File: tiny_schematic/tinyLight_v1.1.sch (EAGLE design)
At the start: 38 parts, among them IC1 NCP1117, IC2 XMEGA-A4TQFP, IC3 CM1293A-02SR, J1 RASM722PX, J2 Molex, J3 PDI, Q1 BC849SMD, Q2 BC849SMD, X1 MICRO-USB

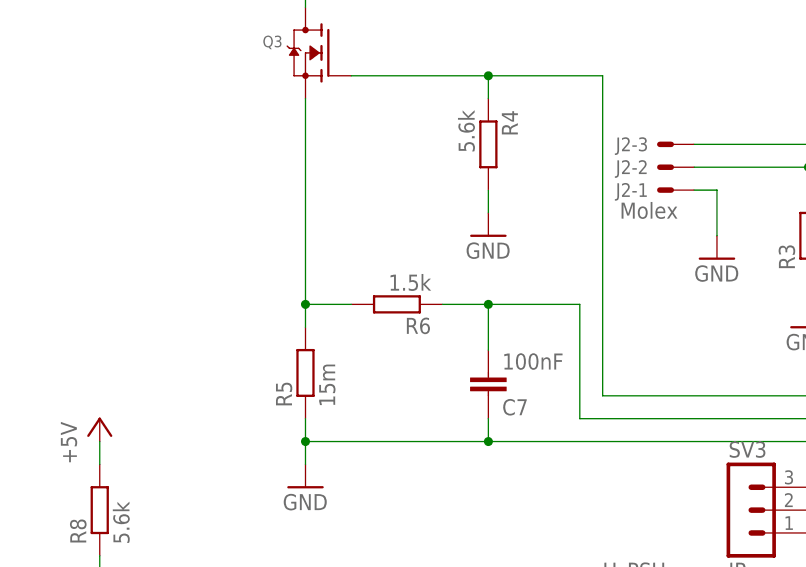
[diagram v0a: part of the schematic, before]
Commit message: Working WS281x implementation (ToDo: Regression Tests)
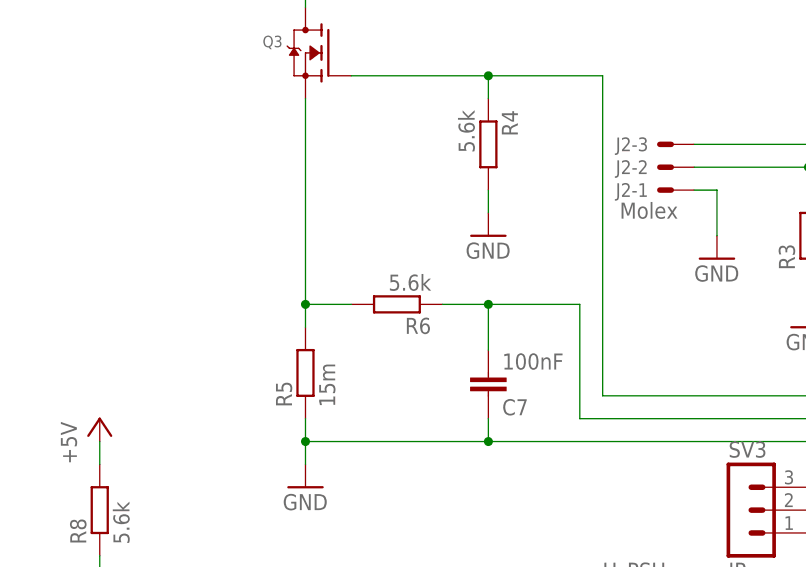
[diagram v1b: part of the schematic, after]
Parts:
- R6: value 1.5k -> 5.6k
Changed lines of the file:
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@@
 <part name="GND14" library="supply1" deviceset="GND" device=""/>
 <part name="GND15" library="supply1" deviceset="GND" device=""/>
-<part name="R6" library="rcl" deviceset="R-EU_" device="M2012" value="1.5k"/>
+<part name="R6" library="rcl" deviceset="R-EU_" device="M2012" value="5.6k"/>
 <part name="C7" library="rcl" deviceset="C-EU" device="C2012" value="100nF"/>
 <part name="FRAME1" library="frames" deviceset="DINA4_L" device=""/>
